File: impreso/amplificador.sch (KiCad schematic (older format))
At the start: 83 parts, among them Q1 2SC3281, Q10 MPSA42, Q11 2SC3281, Q12 2SA1302, Q13 MPSA92, Q14 MPSA92, Q15 MJE340, Q16 MJE350, Q2 MJE340, Q20 2SA1302, Q3 MJE340, Q4 2SC3281, Q6 MJE350, Q7 2SA1302, Q8 MJE350, Q9 MPSA42, T3 TORNILLO, T4 TORNILLO, T5 TORNILLO, T6 TORNILLO, T7 TORNILLO, T8 TORNILLO, U1 MMPQ2222A, U2 MMPQ2907A, U3 LM7809CT, U4 LM7909CT

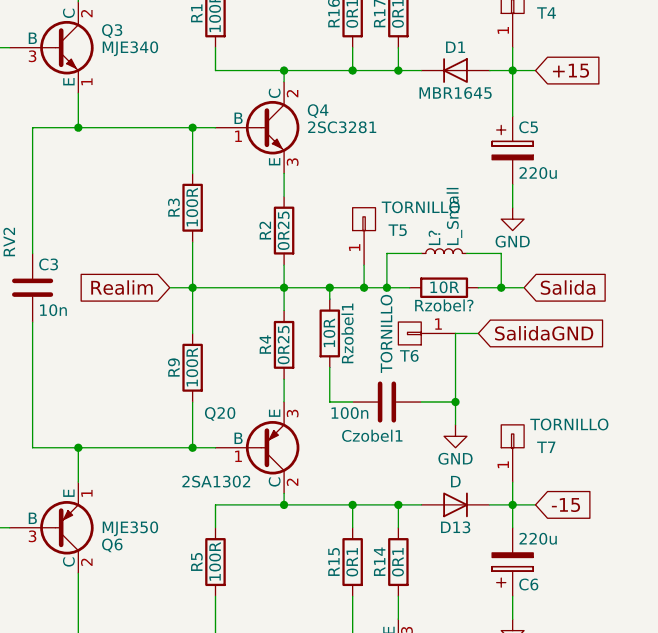
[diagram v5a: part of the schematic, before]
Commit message: Agregué el separador de capacitancia de carga al esquemático y al PCB.
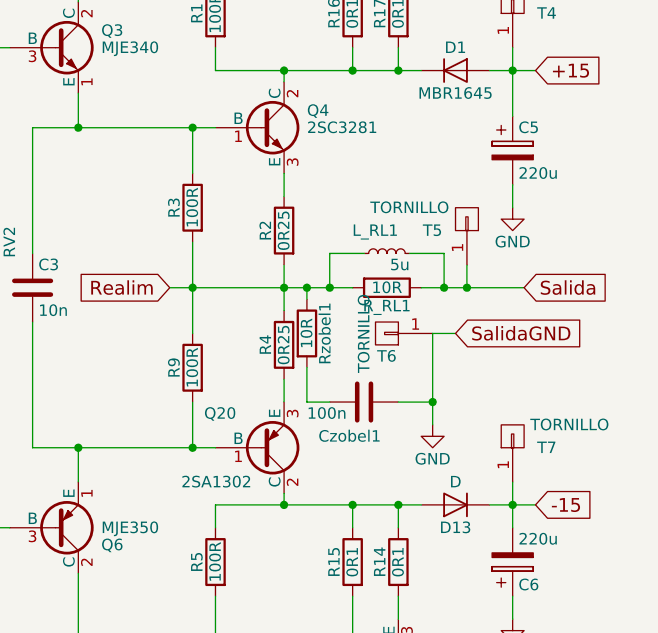
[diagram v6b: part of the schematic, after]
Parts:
- L_RL1: renamed from L?; value L_Small -> 5u; footprint (none) -> Discret:CP4
- gave numbers to parts that had none: 1
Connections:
- net Realim: no longer T5.1 (P1)
- net Salida: now also T5.1 (P1)
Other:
- moved on the sheet: Czobel1, L_RL1, R_RL1, Rzobel1, T5, T6
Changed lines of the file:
@@
 EESchema Schematic File Version 2
-LIBS:power
-LIBS:device
-LIBS:transistors
-LIBS:conn
-LIBS:linear
-LIBS:regul
-LIBS:74xx
-LIBS:cmos4000
-LIBS:adc-dac
-LIBS:memory
-LIBS:xilinx
-LIBS:microcontrollers
-LIBS:dsp
-LIBS:microchip
-LIBS:analog_switches
-LIBS:motorola
-LIBS:texas
-LIBS:intel
-LIBS:audio
-LIBS:interface
-LIBS:digital-audio
-LIBS:philips
-LIBS:display
-LIBS:cypress
-LIBS:siliconi
-LIBS:opto
-LIBS:atmel
-LIBS:contrib
-LIBS:valves
 LIBS:lib_ampli
 LIBS:amplificador-cache
@@
 	1    0    0    -1
 $EndComp
-Text GLabel 9750 3800 2    60   Input ~ 0
+Text GLabel 9650 3800 2    60   Input ~ 0
 SalidaGND
 $Comp
 L GND #PWR06
 U 1 1 559EDF98
-P 9650 4200
-F 0 "#PWR06" H 9650 3950 50  0001 C CNN
-F 1 "GND" H 9650 4050 50  0000 C CNN
-F 2 "" H 9650 4200 60  0000 C CNN
-F 3 "" H 9650 4200 60  0000 C CNN
-	1    9650 4200
+P 9550 4200
+F 0 "#PWR06" H 9550 3950 50  0001 C CNN
+F 1 "GND" H 9550 4050 50  0000 C CNN
+F 2 "" H 9550 4200 60  0000 C CNN
+F 3 "" H 9550 4200 60  0000 C CNN
+	1    9550 4200
 	1    0    0    -1
 $EndComp
@@
 L TORNILLO T6
 U 1 1 559797E2
-P 9450 3800
-F 0 "T6" H 9450 3900 50  0000 C CNN
-F 1 "TORNILLO" V 9550 3800 50  0000 C CNN
-F 2 "bibliotecas:TORNILLO" H 9450 3800 60  0001 C CNN
-F 3 "" H 9450 3800 60  0000 C CNN
-	1    9450 3800
+P 9350 3800
+F 0 "T6" H 9350 3900 50  0000 C CNN
+F 1 "TORNILLO" V 9450 3800 50  0000 C CNN
+F 2 "bibliotecas:TORNILLO" H 9350 3800 60  0001 C CNN
+F 3 "" H 9350 3800 60  0000 C CNN
+	1    9350 3800
 	-1   0    0    1
 $EndComp
@@
 L TORNILLO T5
 U 1 1 55986761
-P 9250 3300
-F 0 "T5" V 9200 3150 50  0000 C CNN
-F 1 "TORNILLO" V 9300 3050 50  0000 C CNN
-F 2 "bibliotecas:TORNILLO" H 9250 3300 60  0001 C CNN
-F 3 "" H 9250 3300 60  0000 C CNN
-	1    9250 3300
-	0    -1   -1   0
+P 9700 3300
+F 0 "T5" V 9650 3150 50  0000 C CNN
+F 1 "TORNILLO" V 9750 3050 50  0000 C CNN
+F 2 "bibliotecas:TORNILLO" H 9700 3300 60  0001 C CNN
+F 3 "" H 9700 3300 60  0000 C CNN
+	1    9700 3300
+	0    1    -1   0
 $EndComp
 $Comp
@@
 	5400 3600 5550 3600
 Wire Wire Line
-	9650 3800 9650 4200
-Wire Wire Line
-	9650 3800 9750 3800
+	9550 3800 9550 4200
+Wire Wire Line
+	9550 3800 9650 3800
 Wire Wire Line
 	1800 3900 1900 3900
@@
 	9900 800  9900 900
 Connection ~ 9900 800
-Wire Wire Line
-	9250 3600 9250 3500
-Connection ~ 9250 3600
 Wire Wire Line
 	6900 6000 6900 5900
@@
 L R Rzobel1
 U 1 1 5670E41C
-P 9100 3800
-F 0 "Rzobel1" V 9180 3800 50  0000 C CNN
-F 1 "10R" V 9100 3800 50  0000 C CNN
-F 2 "Resistors_ThroughHole:Resistor_Horizontal_RM10mm" V 9030 3800 30  0001 C CNN
-F 3 "" H 9100 3800 30  0000 C CNN
-	1    9100 3800
+P 9000 3800
+F 0 "Rzobel1" V 9080 3800 50  0000 C CNN
+F 1 "10R" V 9000 3800 50  0000 C CNN
+F 2 "Resistors_ThroughHole:Resistor_Horizontal_RM10mm" V 8930 3800 30  0001 C CNN
+F 3 "" H 9000 3800 30  0000 C CNN
+	1    9000 3800
 	1    0    0    -1
 $EndComp
@@
 L C Czobel1
 U 1 1 5670E6F6
-P 9350 4100
-F 0 "Czobel1" V 9500 3900 50  0000 L CNN
-F 1 "100n" V 9400 3850 50  0000 L CNN
-F 2 "Capacitors_ThroughHole:C_Rect_L7_W3.5_P5" H 9388 3950 30  0001 C CNN
-F 3 "" H 9350 4100 60  0000 C CNN
-	1    9350 4100
+P 9250 4100
+F 0 "Czobel1" V 9400 3900 50  0000 L CNN
+F 1 "100n" V 9300 3850 50  0000 L CNN
+F 2 "Capacitors_ThroughHole:C_Rect_L7_W3.5_P5" H 9288 3950 30  0001 C CNN
+F 3 "" H 9250 4100 60  0000 C CNN
+	1    9250 4100
 	0    1    1    0
 $EndComp
 Wire Wire Line
-	9100 3650 9100 3600
-Connection ~ 9100 3600
-Wire Wire Line
-	9100 3950 9100 4100
-Wire Wire Line
-	9100 4100 9200 4100
-Wire Wire Line
-	9650 4100 9500 4100
-Connection ~ 9650 4100
+	9000 3600 9000 3650
+Connection ~ 9000 3600
+Wire Wire Line
+	9000 3950 9000 4100
+Wire Wire Line
+	9000 4100 9100 4100
+Wire Wire Line
+	9550 4100 9400 4100
+Connection ~ 9550 4100
 $Comp
 L R R21
@@
 Connection ~ 6000 1500
 $Comp
-L R Rzobel?
+L R R_RL1
 U 1 1 56726E0F
-P 9600 3600
-F 0 "Rzobel?" V 9680 3600 50  0000 C CNN
-F 1 "10R" V 9600 3600 50  0000 C CNN
-F 2 "Resistors_ThroughHole:Resistor_Horizontal_RM10mm" V 9530 3600 30  0001 C CNN
-F 3 "" H 9600 3600 30  0000 C CNN
-	1    9600 3600
+P 9350 3600
+F 0 "R_RL1" V 9430 3600 50  0000 C CNN
+F 1 "10R" V 9350 3600 50  0000 C CNN
+F 2 "Resistors_ThroughHole:Resistor_Horizontal_RM10mm" V 9280 3600 30  0001 C CNN
+F 3 "" H 9350 3600 30  0000 C CNN
+	1    9350 3600
 	0    1    1    0
 $EndComp
 Wire Wire Line
-	8400 3600 9450 3600
-Wire Wire Line
-	9350 3600 9350 3450
-Wire Wire Line
-	9350 3450 9500 3450
-Connection ~ 9350 3600
-Wire Wire Line
-	9750 3600 9950 3600
-Wire Wire Line
-	9700 3450 9850 3450
-Wire Wire Line
-	9850 3450 9850 3600
-Connection ~ 9850 3600
-$Comp
-L L_Small L?
+	9100 3600 9100 3450
+Wire Wire Line
+	9100 3450 9250 3450
+Connection ~ 9100 3600
+Wire Wire Line
+	9450 3450 9600 3450
+Wire Wire Line
+	9600 3450 9600 3600
+Connection ~ 9600 3600
+$Comp
+L L_Small L_RL1
 U 1 1 5672A668
-P 9600 3450
-F 0 "L?" H 9630 3490 50  0000 L CNN
-F 1 "L_Small" H 9630 3410 50  0000 L CNN
-F 2 "" H 9600 3450 50  0000 C CNN
-F 3 "" H 9600 3450 50  0000 C CNN
-	1    9600 3450
+P 9350 3450
+F 0 "L_RL1" V 9450 3400 50  0000 L CNN
+F 1 "5u" V 9300 3350 50  0000 L CNN
+F 2 "Discret:CP4" H 9350 3450 50  0001 C CNN
+F 3 "" H 9350 3450 50  0000 C CNN
+	1    9350 3450
 	0    -1   -1   0
 $EndComp
 Entry Wire Line
 	6140 1790 6240 1890
+Wire Wire Line
+	8400 3600 9200 3600
+Wire Wire Line
+	9500 3600 9950 3600
+Wire Wire Line
+	9700 3500 9700 3600
+Connection ~ 9700 3600
 $EndSCHEMATC

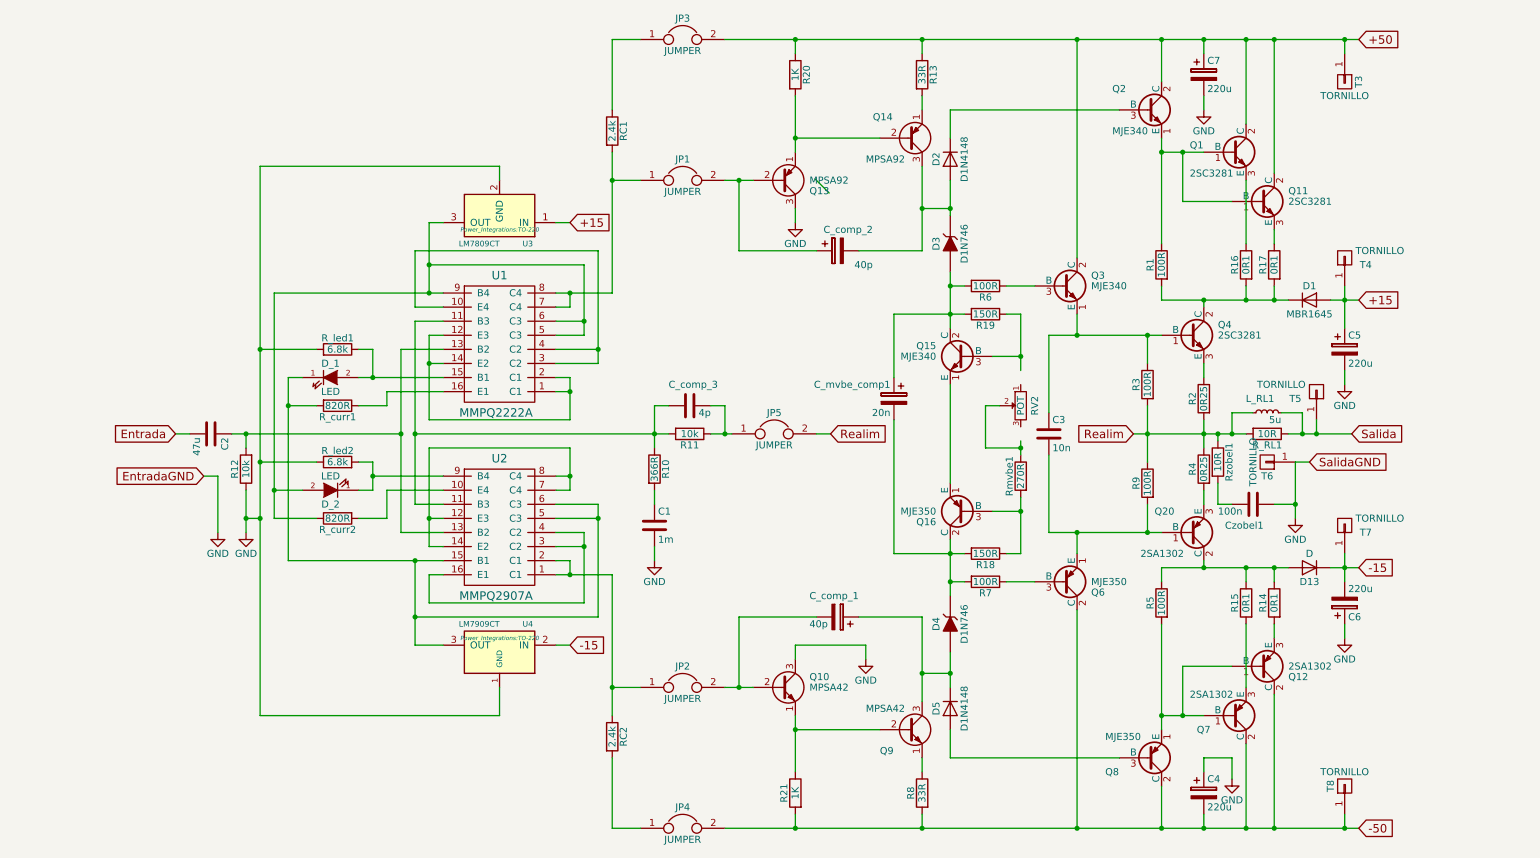
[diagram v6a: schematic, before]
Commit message: Se hizo el ruteo con los nuevos componentes, y se corrigieron los valores de las protecciones, corrigiendo las disparidades.
Ya se mandó el circuito al LCI, para hacer.
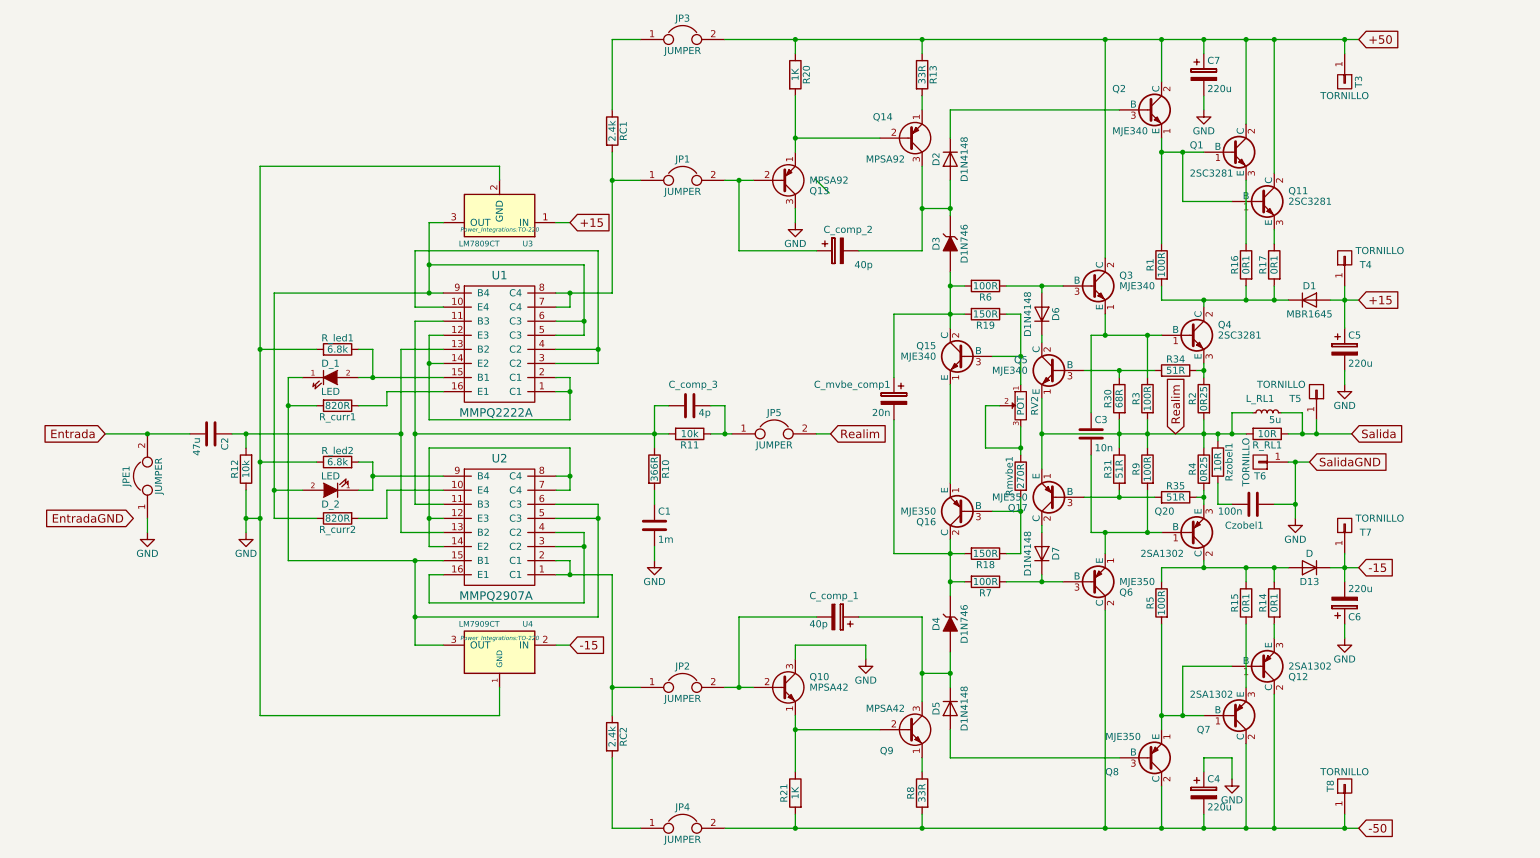
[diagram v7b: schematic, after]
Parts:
- added D6, D7: D1N4148, Diodes_ThroughHole:Diode_DO-35_SOD27_Horizontal_RM10, symbol D
- added JPE1: JUMPER, Pin_Headers:Pin_Header_Straight_1x02, symbol JUMPER
- added Q17: MJE350, TO_SOT_Packages_THT:SOT126_SOT32_Housing_Vertical, symbol BD136
- added Q5: MJE340, TO_SOT_Packages_THT:SOT126_SOT32_Housing_Vertical, symbol BD135
- added R30: 68R, Resistors_ThroughHole:Resistor_Horizontal_RM10mm, symbol R
- added R31, R34, R35: 51R, Resistors_ThroughHole:Resistor_Horizontal_RM10mm, symbol R
- Q10, Q13, Q14, Q9: footprint TO_SOT_Packages_THT:TO-92_Horizontal1_Inline_Narrow_Oval -> TO_SOT_Packages_THT:TO-92_Inline_Narrow_Oval
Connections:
- net Entrada: now also JPE1.2
- net GND: now also JPE1.1
- net Realim: now also Q17.1 (E), Q5.1 (E), R30.2, R31.1
- net at RV2.2, Rmvbe1.1: now also RV2.3
- net at RV2.1: now also Q15.3 (B), R19.1
- net at Q3.3 (B), R6.1: now also D6.2 (A)
- net at Q6.3 (B), R7.1: now also D7.1 (K)
- net at Q4.3 (E), R2.1: now also R34.1
- net at Q20.3 (E), R4.2: now also R35.1
- new net: Q17.3 (B), R31.2, R35.2
- new net: Q5.3 (B), R30.1, R34.2
- new net: D7.2 (A), Q17.2 (C)
- new net: D6.1 (K), Q5.2 (C)
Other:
- moved on the sheet: C3, Q3, Q6, R3, R9, T6

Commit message: Ensanché las vías del PCB y agregué un par de vías.
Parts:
- D_1, D_2: symbol LED -> LED-RESCUE-amplificador
- RV2: symbol POT -> POT-RESCUE-amplificador
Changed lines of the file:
@@
 LIBS:lib_ampli
 LIBS:amplificador-cache
-EELAYER 25 0
+EELAYER 26 0
 EELAYER END
 $Descr A4 11693 8268
@@
 $EndComp
 $Comp
-L POT RV2
+L POT-RESCUE-amplificador RV2
 U 1 1 55954B79
 P 7600 3400
@@
 $EndComp
 $Comp
-L LED D_1
+L LED-RESCUE-amplificador D_1
 U 1 1 567201A4
 P 2700 3200
@@
 $EndComp
 $Comp
-L LED D_2
+L LED-RESCUE-amplificador D_2
 U 1 1 5672D9F0
 P 2700 4000
